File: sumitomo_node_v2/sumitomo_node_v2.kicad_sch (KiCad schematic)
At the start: 15 parts, among them SW1 SW_DIP_x10, U1 Arduino_Mega_2560_Without_Bot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, U2 PN532_SPI_Uart_Breakout_Board, U3 HC12

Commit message: Update library paths and unsaved changes to `sumitomo_node_v2`.
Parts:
- H1, H2, H3, H4: footprint MountingHole:MountingHole_5.3mm_M5_DIN965_Pad -> MountingHole:MountingHole_5.3mm_M5_ISO7380
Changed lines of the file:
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@@
 			)
 		)
-		(property "Footprint" "MountingHole:MountingHole_5.3mm_M5_DIN965_Pad"
+		(property "Footprint" "MountingHole:MountingHole_5.3mm_M5_ISO7380"
 			(at 45.72 158.7499 0)
 			(effects
@@
 			)
 		)
-		(property "Footprint" "MountingHole:MountingHole_5.3mm_M5_DIN965_Pad"
+		(property "Footprint" "MountingHole:MountingHole_5.3mm_M5_ISO7380"
 			(at 45.72 171.4499 0)
 			(effects
@@
 			)
 		)
-		(property "Footprint" "MountingHole:MountingHole_5.3mm_M5_DIN965_Pad"
+		(property "Footprint" "MountingHole:MountingHole_5.3mm_M5_ISO7380"
 			(at 45.72 152.4 0)
 			(effects
@@
 			)
 		)
-		(property "Footprint" "MountingHole:MountingHole_5.3mm_M5_DIN965_Pad"
+		(property "Footprint" "MountingHole:MountingHole_5.3mm_M5_ISO7380"
 			(at 45.72 165.0999 0)
 			(effects

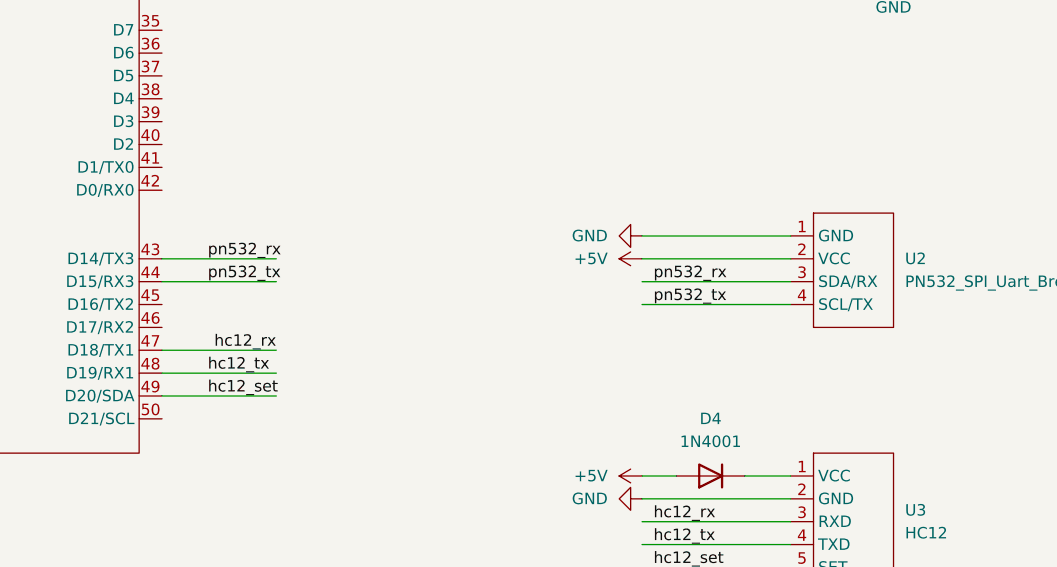
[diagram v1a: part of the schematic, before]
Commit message: Fix PN532 UART and re-route to Serial2.
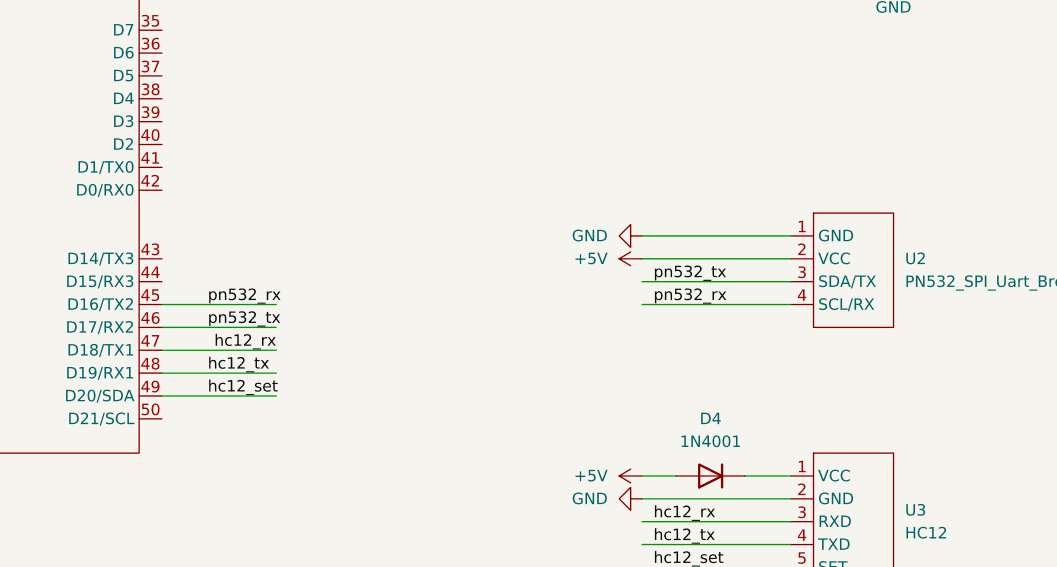
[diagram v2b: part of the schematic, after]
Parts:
- H1, H2, H3, H4: footprint MountingHole:MountingHole_5.3mm_M5_ISO7380 -> MountingHole:MountingHole_3.2mm_M3_ISO7380
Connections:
- net pn532_rx: now also U1.45 (D16/TX2), U2.4 (SCL/RX); no longer U1.43 (D14/TX3), U2.3 (SDA/RX)
- net pn532_tx: now also U1.46 (D17/RX2), U2.3 (SDA/TX); no longer U1.44 (D15/RX3), U2.4 (SCL/TX)
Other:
- title: Sumitomo Node v2 -> Sumitomo Node v2.1
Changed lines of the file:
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@@
 	(paper "A4")
 	(title_block
-		(title "Sumitomo Node v2")
+		(title "Sumitomo Node v2.1")
 		(company "Cirotec Automation")
 	)
@@
 	(wire
 		(pts
+			(xy 107.95 104.14) (xy 120.65 104.14)
+		)
+		(stroke
+			(width 0)
+			(type default)
+		)
+	)
+	(wire
+		(pts
 			(xy 48.26 99.06) (xy 63.5 99.06)
 		)
@@
 	(wire
 		(pts
-			(xy 107.95 99.06) (xy 120.65 99.06)
-		)
-		(stroke
-			(width 0)
-			(type default)
-		)
-	)
-	(wire
-		(pts
-			(xy 107.95 96.52) (xy 120.65 96.52)
-		)
-		(stroke
-			(width 0)
-			(type default)
-		)
-	)
-	(wire
-		(pts
 			(xy 154.94 57.15) (xy 168.91 57.15)
 		)
@@
 	(wire
 		(pts
+			(xy 107.95 101.6) (xy 120.65 101.6)
+		)
+		(stroke
+			(width 0)
+			(type default)
+		)
+	)
+	(wire
+		(pts
 			(xy 48.26 106.68) (xy 63.5 106.68)
 		)
@@
 			(width 0)
 			(type default)
-		)
-	)
-	(label "pn532_tx"
-		(at 113.03 99.06 0)
-		(fields_autoplaced yes)
-		(effects
-			(font
-				(size 1.27 1.27)
-			)
-			(justify left bottom)
 		)
 	)
@@
 		)
 	)
-	(label "pn532_rx"
+	(label "pn532_tx"
 		(at 162.56 99.06 0)
 		(fields_autoplaced yes)
@@
 		)
 	)
-	(label "pn532_tx"
+	(label "pn532_rx"
 		(at 162.56 101.6 0)
 		(fields_autoplaced yes)
@@
 		)
 	)
+	(label "pn532_tx"
+		(at 113.03 104.14 0)
+		(fields_autoplaced yes)
+		(effects
+			(font
+				(size 1.27 1.27)
+			)
+			(justify left bottom)
+		)
+	)
 	(label "sw_8"
 		(at 49.53 91.44 0)
@@
 		)
 	)
+	(label "pn532_rx"
+		(at 113.03 101.6 0)
+		(fields_autoplaced yes)
+		(effects
+			(font
+				(size 1.27 1.27)
+			)
+			(justify left bottom)
+		)
+	)
 	(label "sw_3"
 		(at 49.53 104.14 0)
@@
 	(label "led_yellow"
 		(at 49.53 77.47 0)
-		(fields_autoplaced yes)
-		(effects
-			(font
-				(size 1.27 1.27)
-			)
-			(justify left bottom)
-		)
-	)
-	(label "pn532_rx"
-		(at 113.03 96.52 0)
 		(fields_autoplaced yes)
 		(effects
@@
 			)
 		)
-		(property "Footprint" "MountingHole:MountingHole_5.3mm_M5_ISO7380"
+		(property "Footprint" "MountingHole:MountingHole_3.2mm_M3_ISO7380"
 			(at 45.72 158.7499 0)
 			(effects
@@
 			)
 		)
-		(property "Footprint" "MountingHole:MountingHole_5.3mm_M5_ISO7380"
+		(property "Footprint" "MountingHole:MountingHole_3.2mm_M3_ISO7380"
 			(at 45.72 171.4499 0)
 			(effects
@@
 			)
 		)
-		(property "Footprint" "MountingHole:MountingHole_5.3mm_M5_ISO7380"
+		(property "Footprint" "MountingHole:MountingHole_3.2mm_M3_ISO7380"
 			(at 45.72 152.4 0)
 			(effects
@@
 			)
 		)
-		(property "Footprint" "MountingHole:MountingHole_5.3mm_M5_ISO7380"
+		(property "Footprint" "MountingHole:MountingHole_3.2mm_M3_ISO7380"
 			(at 45.72 165.0999 0)
 			(effects
